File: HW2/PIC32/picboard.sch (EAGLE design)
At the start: 22 parts, among them J1 USB

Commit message: Finished schematic
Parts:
- renumbered U$3 to .
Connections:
- removed net A4/LED: LED2.A, U$4.12.LED/A4
- removed net N$10: J2.5
- removed net N$11: J2.4
- removed net N$12: J2.3
- removed net N$13: J2.2
- removed net N$14: J2.1
- removed net N$15: J3.8
- removed net N$16: J3.7
- removed net N$17: J3.6
- removed net N$18: J3.5
- removed net N$19: J3.4
- removed net N$20: J3.3
- removed net N$21: J3.2
- removed net N$22: J3.1
- removed net N$7: J2.8
- removed net N$8: J2.7
- removed net N$9: J2.6
- new net A0: J3.8, U$4.2.A0
- new net A1: J3.7, U$4.3.A1
- new net B13: J2.6, U$4.24.B13
- new net B14: J2.7, U$4.25.B14
- new net B15: J2.8, U$4.26.B15
- new net B2: J3.6, U$4.6.B2
- new net B3: J3.5, U$4.7.B3
- new net B7: J2.3, U$4.16.B7
- new net B8: J2.4, U$4.17.B8
- new net B9: J2.5, U$4.18.B9
- new net LED/A4: J3.3, LED2.A, U$4.12.LED/A4
- net +3V3: now also J3.2
- net +5V: now also J2.2
- net GND: now also J2.1, J3.1
- net USER/B4: now also J3.4
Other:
- moved on the sheet: C2, C3, J2, J3, LED1, R1, U$2

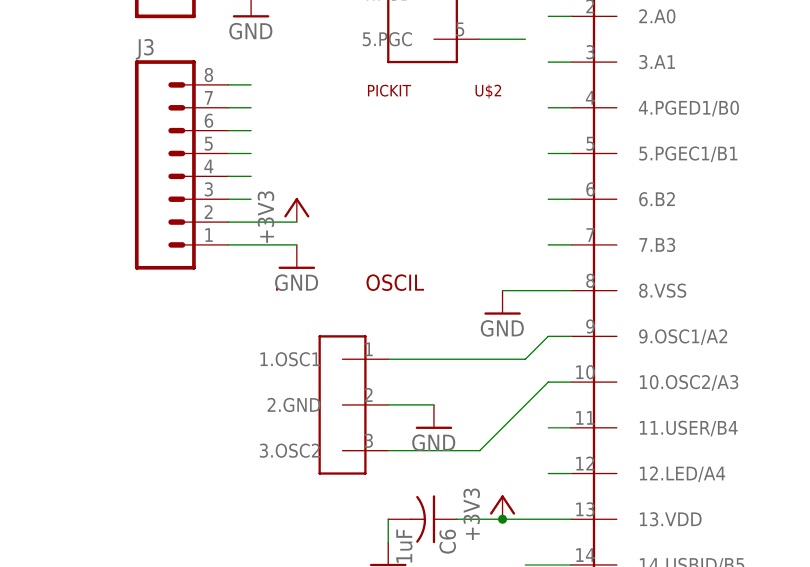
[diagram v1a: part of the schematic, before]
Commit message: finished PCB .brd layout. Still need to error check
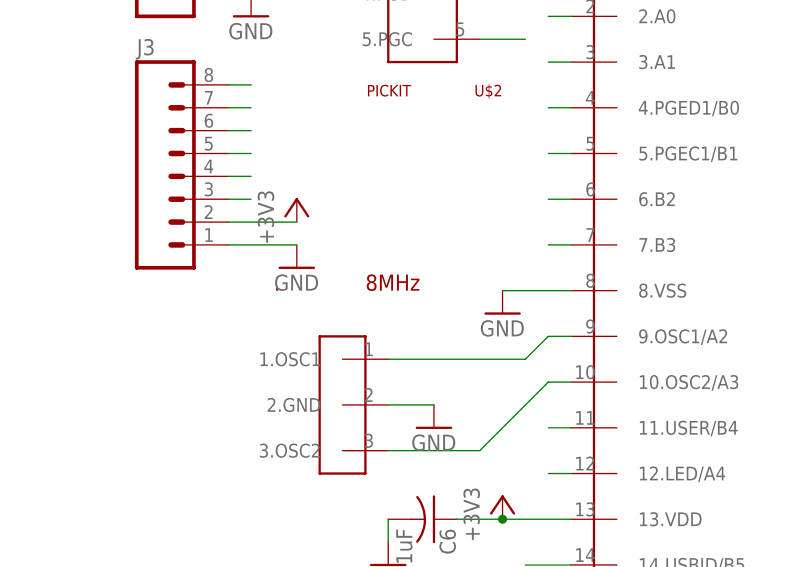
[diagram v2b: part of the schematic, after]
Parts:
- .: value OSCIL -> 8MHz
- C2, C4: device PIC32:CPOL-USB45181B -> PIC32:CPOL-USB45181A
- R1, R2, R3, R4: device PIC32:R-US_0411/15 -> PIC32:R-US_0207/10
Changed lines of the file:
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@@
 <part name="C1" library="PIC32" deviceset="C-US" device="025-025X050" value="0.1uF"/>
 <part name="GND8" library="PIC32" deviceset="GND" device=""/>
-<part name="C2" library="PIC32" deviceset="CPOL-US" device="B45181B" value="10uF"/>
+<part name="C2" library="PIC32" deviceset="CPOL-US" device="B45181A" value="10uF"/>
 <part name="C3" library="PIC32" deviceset="C-US" device="025-025X050" value="0.1uF"/>
 <part name="GND9" library="PIC32" deviceset="GND" device=""/>
@@
 <part name="+3V4" library="PIC32" deviceset="+3V3" device=""/>
 <part name="LED1" library="PIC32" deviceset="LED" device="3MM" value="red"/>
-<part name="R1" library="PIC32" deviceset="R-US_" device="0411/15" value="330"/>
+<part name="R1" library="PIC32" deviceset="R-US_" device="0207/10" value="330"/>
 <part name="GND11" library="PIC32" deviceset="GND" device=""/>
 <part name="LED2" library="PIC32" deviceset="LED" device="3MM" value="green"/>
-<part name="R2" library="PIC32" deviceset="R-US_" device="0411/15" value="330"/>
+<part name="R2" library="PIC32" deviceset="R-US_" device="0207/10" value="330"/>
 <part name="GND12" library="PIC32" deviceset="GND" device=""/>
 <part name="USER" library="PIC32" deviceset="PBUTTON" device=""/>
@@
 <part name="GND13" library="PIC32" deviceset="GND" device=""/>
 <part name="GND14" library="PIC32" deviceset="GND" device=""/>
-<part name="R3" library="PIC32" deviceset="R-US_" device="0411/15" value="10k"/>
-<part name="R4" library="PIC32" deviceset="R-US_" device="0411/15" value="10k"/>
+<part name="R3" library="PIC32" deviceset="R-US_" device="0207/10" value="10k"/>
+<part name="R4" library="PIC32" deviceset="R-US_" device="0207/10" value="10k"/>
 <part name="+3V5" library="PIC32" deviceset="+3V3" device=""/>
 <part name="+3V6" library="PIC32" deviceset="+3V3" device=""/>
@@
 <part name="+3V7" library="PIC32" deviceset="+3V3" device=""/>
 <part name="GND15" library="PIC32" deviceset="GND" device=""/>
-<part name="C4" library="PIC32" deviceset="CPOL-US" device="B45181B" value="10uF"/>
+<part name="C4" library="PIC32" deviceset="CPOL-US" device="B45181A" value="10uF"/>
 <part name="P+2" library="PIC32" deviceset="+5V" device=""/>
 <part name="C5" library="PIC32" deviceset="C-US" device="025-025X050" value="0.1uF"/>
-<part name="." library="PIC32" deviceset="OSCIL" device=""/>
+<part name="." library="PIC32" deviceset="OSCIL" device="" value="8MHz"/>
 <part name="GND16" library="supply1" deviceset="GND" device=""/>
 <part name="C6" library="PIC32" deviceset="C-US" device="025-025X050" value="0.1uF"/>
